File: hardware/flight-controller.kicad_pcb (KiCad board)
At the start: 4 copper layers, 70 x 70 mm, 111 parts, among them J1 USB_C_Receptacle_USB2.0_16P, J10 Screw_Terminal_01x02, J11 Micro_SD_Card_Det_Hirose_DM3AT, J12 Conn_01x03, J13 Conn_01x03, J14 Conn_01x03, J15 Conn_01x03, J16 Screw_Terminal_01x02, J17 Conn_01x04, J18 Screw_Terminal_01x02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

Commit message: finished board
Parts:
- added C39: 100nF, Capacitor_SMD:C_0402_1005Metric, F.Cu at (166.0, 114.7)
- added SET1: SW_Push, Button_Switch_SMD:SW_Push_SPST_NO_Alps_SKRK, F.Cu at (165.9, 117.0)
- BZ1: value Buzzer -> PKMCS0909E4000-R1
- J10, J16, J18, J5, J7, J9: footprint TerminalBlock_4Ucon:TerminalBlock_4Ucon_1x02_P3.50mm_Horizontal -> TerminalBlock:TerminalBlock_MaiXu_MX126-5.0-02P_1x02_P5.00mm
- moved J7 5.55 mm to (112.0, 76.5), turned to 90 degrees
- moved J16 5.05 mm to (172.0, 129.8), turned to -90 degrees
- moved J18 4.35 mm to (122.5, 73.0), turned to 0 degrees
- moved J5 4.35 mm to (156.5, 73.0), turned to 0 degrees
- moved J9 3.09 mm to (112.0, 134.2), turned to 90 degrees
- moved J10 2.86 mm to (172.0, 72.0), turned to -90 degrees
- moved C37 2.57 mm to (166.5, 131.0), turned to -90 degrees
- moved C36 2.36 mm to (166.5, 75.0), turned to -90 degrees
- moved C34 1.77 mm to (117.5, 74.0), turned to 90 degrees
- moved C35 1.60 mm to (117.5, 132.0), turned to 90 degrees
- moved C32 1.25 mm to (125.0, 78.5), turned to 0 degrees
- moved C33 1.25 mm to (159.0, 78.5), turned to 0 degrees
- moved J12 0.50 mm to (120.5, 130.5)
- moved J13 0.50 mm to (125.1, 130.5)
- moved J14 0.50 mm to (129.7, 130.5)
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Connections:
- U7 pad 89: unconnected-(U7-PB3(JTDO-Pad89) -> /SET_BTN
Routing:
- net /SET_BTN: track 0.00 -> 26.0 mm, vias 0 -> 2
- net +BATT: track 39.7 -> 43.4 mm
- net GND: track 92.8 -> 94.9 mm, vias 186 -> 188
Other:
- board text added: "+"
- board text added: "-"
- board text added: "12V"
- board text added: "3.3V"
- board text added: "CLK"
- board text added: "IO"
- board text added: "SWD"

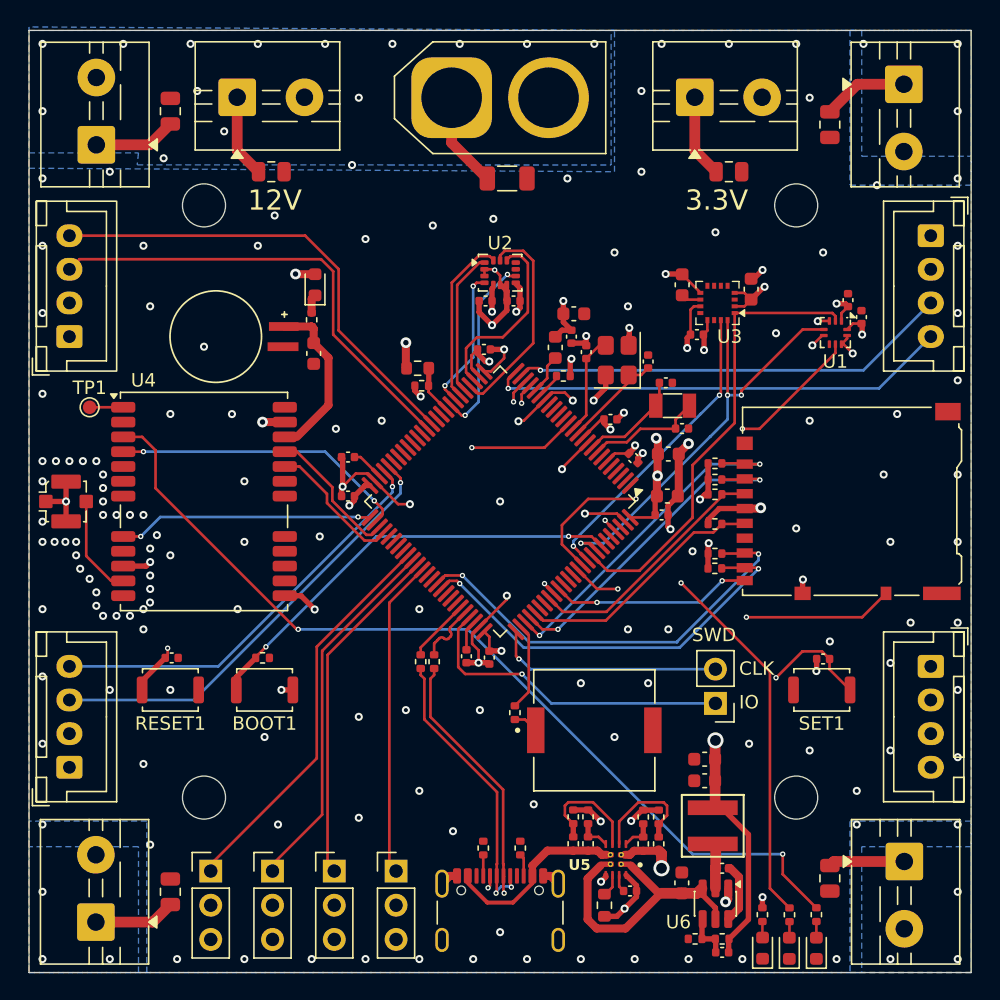
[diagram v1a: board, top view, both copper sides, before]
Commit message: added I2C pins
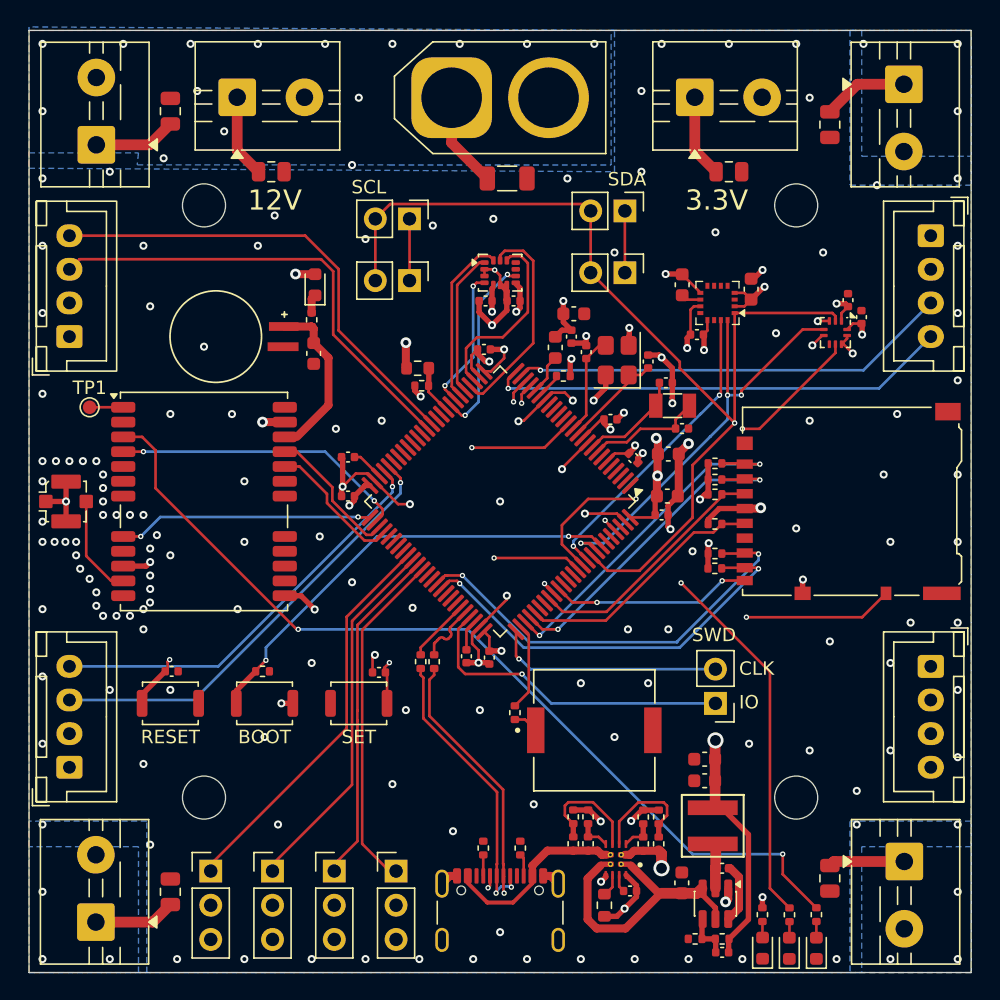
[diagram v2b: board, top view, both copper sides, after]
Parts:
- added J20: Conn_01x02, Connector_PinHeader_2.54mm:PinHeader_1x02_P2.54mm_Vertical, F.Cu at (135.3, 82.0)
- added J21: Conn_01x02, Connector_PinHeader_2.54mm:PinHeader_1x02_P2.54mm_Vertical, F.Cu at (135.3, 86.6)
- added J22: Conn_01x02, Connector_PinHeader_2.54mm:PinHeader_1x02_P2.54mm_Vertical, F.Cu at (151.3, 81.4)
- added J23: Conn_01x02, Connector_PinHeader_2.54mm:PinHeader_1x02_P2.54mm_Vertical, F.Cu at (151.3, 86.0)
- moved SET1 34.4 mm to (131.5, 118.0)
- moved C39 33.0 mm to (133.0, 115.7)
- moved BOOT1 1.00 mm to (124.5, 118.0)
- moved C11 1.00 mm to (117.6, 115.6)
- moved R16 1.00 mm to (124.3, 115.6)
- moved RESET1 1.00 mm to (117.5, 118.0)
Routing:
- net /SCL: track 34.0 -> 75.5 mm, vias 0 -> 1
- net /SDA: track 32.9 -> 71.7 mm
- net /SET_BTN: track 26.0 -> 20.6 mm
- net GND: track 94.9 -> 100.1 mm, vias 188 -> 189
- net /PWM_4: track 23.4 -> 25.1 mm
- net /BOOT: track 32.8 -> 33.7 mm
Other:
- board text added: "BOOT"
- board text added: "RESET"
- board text added: "SCL"
- board text added: "SDA"
- board text added: "SET"

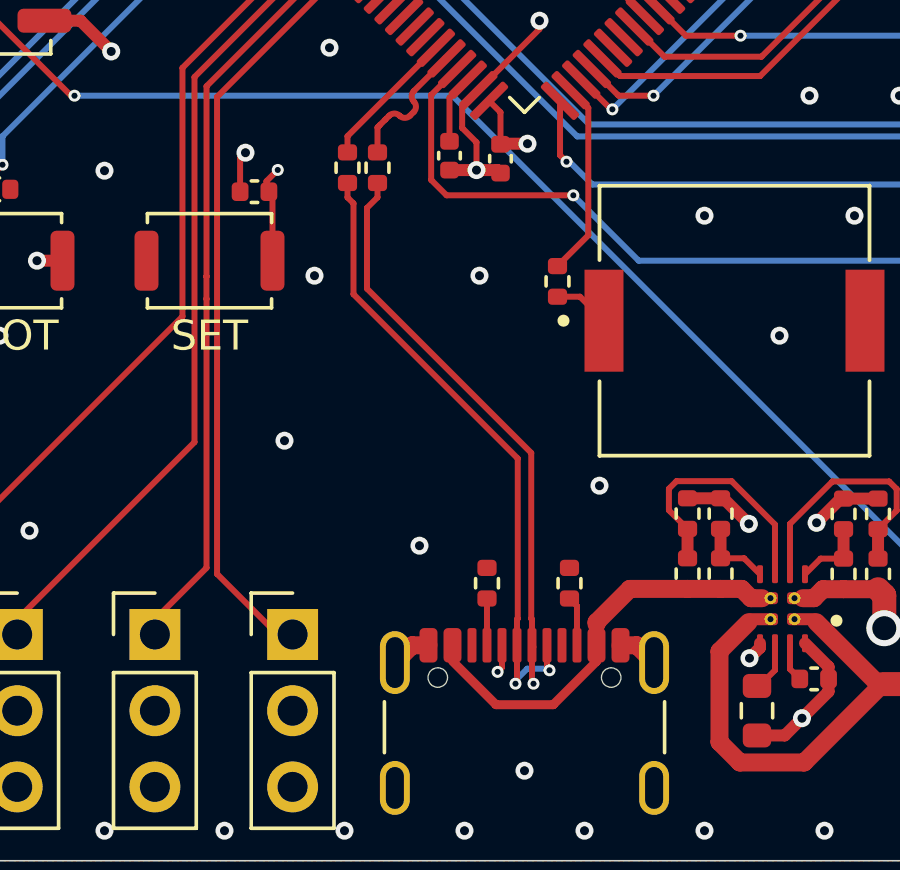
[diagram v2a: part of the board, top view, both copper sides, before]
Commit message: fixed usb plug
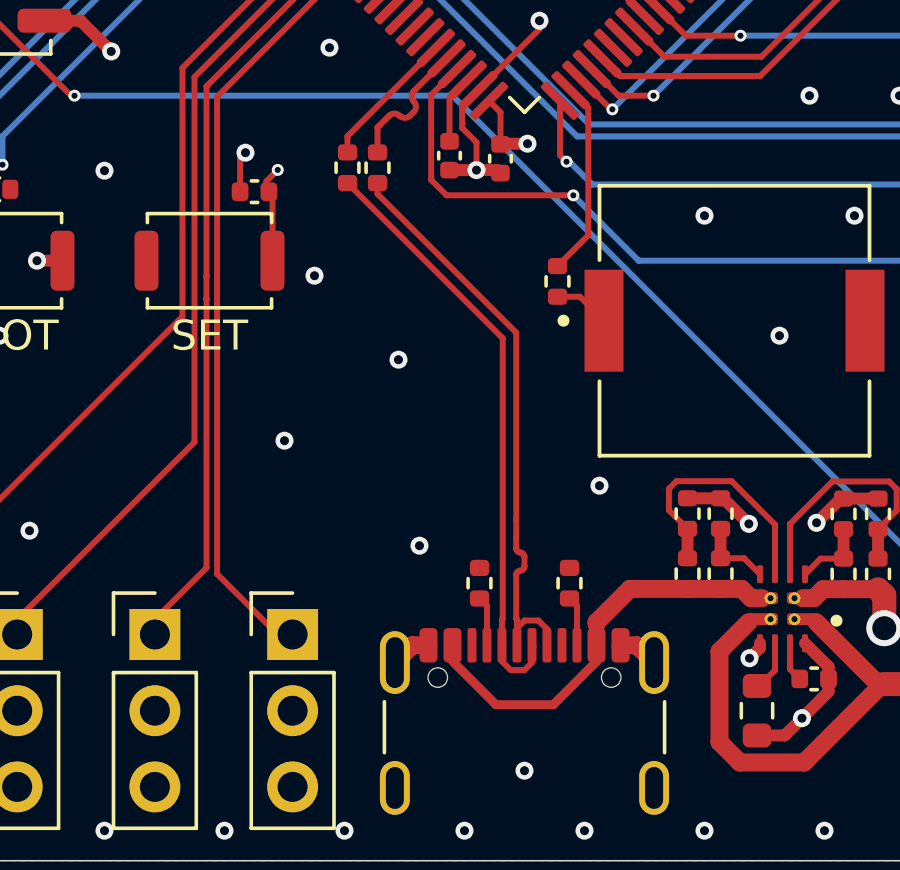
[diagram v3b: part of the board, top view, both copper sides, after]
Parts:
- moved R1 0.25 mm to (140.5, 128.8)
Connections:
- J1 pad A6: /USB_- -> /USB_+
- J1 pad A7: /USB_+ -> /USB_-
- J1 pad B6: /USB_- -> /USB_+
- J1 pad B7: /USB_+ -> /USB_-
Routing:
- net /USB_+: track 21.7 -> 20.0 mm, vias 2 -> 0
- net /USB_-: track 21.4 -> 20.0 mm, vias 2 -> 0
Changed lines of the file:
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@@
 			(layers "F.Cu" "F.Mask" "F.Paste")
 			(roundrect_rratio 0.25)
-			(net 28 "/USB_-")
+			(net 26 "/USB_+")
 			(pinfunction "D+")
 			(pintype "bidirectional")
@@
 			(layers "F.Cu" "F.Mask" "F.Paste")
 			(roundrect_rratio 0.25)
-			(net 26 "/USB_+")
+			(net 28 "/USB_-")
 			(pinfunction "D-")
 			(pintype "bidirectional")
@@
 			(layers "F.Cu" "F.Mask" "F.Paste")
 			(roundrect_rratio 0.25)
-			(net 28 "/USB_-")
+			(net 26 "/USB_+")
 			(pinfunction "D+")
 			(pintype "bidirectional")
@@
 			(layers "F.Cu" "F.Mask" "F.Paste")
 			(roundrect_rratio 0.25)
-			(net 26 "/USB_+")
+			(net 28 "/USB_-")
 			(pinfunction "D-")
 			(pintype "bidirectional")
@@
 	(footprint "Resistor_SMD:R_0402_1005Metric"
 		(layer "F.Cu")
-		(at 140.75 128.75 90)
+		(at 140.5 128.75 90)
 		(descr "Resistor SMD 0402 (1005 Metric), square (rectangular) end terminal, IPC-7351 nominal, (Body size source: IPC-SM-782 page 72, https://www.pcb-3d.com/wordpress/wp-content/uploads/ipc-sm-782a_amendment_1_and_2.pdf), generated with kicad-footprint-generator")
 		(tags "resistor")
@@
 	)
 	(via
-		(at 140.5 118.5)
+		(at 137.8 121.3)
 		(size 0.6)
 		(drill 0.3)
@@
 	)
 	(segment
-		(start 142.225 129.932499)
-		(end 142.25 129.957499)
+		(start 142.75 130.281888)
+		(end 142.75 130.82)
 		(width 0.2)
 		(layer "F.Cu")
@@
 	)
 	(segment
-		(start 136.75 116.24)
-		(end 136.75 118.931802)
+		(start 141.725 127.265204)
+		(end 141.725 126.605964)
 		(width 0.2)
 		(layer "F.Cu")
@@
 	)
 	(segment
-		(start 136.75 118.931802)
-		(end 142.225 124.406802)
+		(start 137.1 115.773602)
+		(end 137.1 115.409999)
 		(width 0.2)
 		(layer "F.Cu")
@@
 	)
 	(segment
-		(start 141.25 131.558683)
-		(end 141.103508 131.705175)
+		(start 141.75 130.245001)
+		(end 142.001001 129.994)
 		(width 0.2)
 		(layer "F.Cu")
@@
 	)
 	(segment
-		(start 137.1 115.409999)
-		(end 137.1 115.89)
+		(start 141.725 127.591352)
+		(end 141.725 127.265204)
 		(width 0.2)
 		(layer "F.Cu")
@@
 	)
 	(segment
-		(start 142.25 132.049997)
-		(end 142.300003 132.1)
+		(start 141.75 129.957499)
+		(end 141.725 129.932499)
 		(width 0.2)
 		(layer "F.Cu")
@@
 	)
 	(segment
-		(start 142.225 124.406802)
-		(end 142.225 129.932499)
+		(start 141.998852 128.191352)
+		(end 141.998852 127.865204)
 		(width 0.2)
 		(layer "F.Cu")
@@
 	)
 	(segment
-		(start 142.25 129.957499)
-		(end 142.25 130.82)
+		(start 141.75 130.82)
+		(end 141.75 130.245001)
 		(width 0.2)
 		(layer "F.Cu")
@@
 	)
 	(segment
-		(start 141.25 130.82)
-		(end 141.25 131.558683)
+		(start 141.725 126.605964)
+		(end 141.725 120.398602)
 		(width 0.2)
 		(layer "F.Cu")
@@
 	)
 	(segment
-		(start 142.3 130.87)
-		(end 142.25 130.82)
+		(start 141.725 120.398602)
+		(end 137.1 115.773602)
 		(width 0.2)
 		(layer "F.Cu")
@@
 	)
 	(segment
-		(start 137.1 115.89)
-		(end 136.75 116.24)
+		(start 142.462112 129.994)
+		(end 142.75 130.281888)
 		(width 0.2)
 		(layer "F.Cu")
@@
 	)
 	(segment
-		(start 142.25 130.82)
-		(end 142.25 132.049997)
+		(start 142.001001 129.994)
+		(end 142.462112 129.994)
 		(width 0.2)
 		(layer "F.Cu")
 		(net 26)
 	)
-	(via
-		(at 141.103508 131.705175)
-		(size 0.4)
-		(drill 0.2)
-		(layers "F.Cu" "B.Cu")
-		(net 26)
-	)
-	(via
-		(at 142.300003 132.1)
-		(size 0.4)
-		(drill 0.2)
-		(layers "F.Cu" "B.Cu")
-		(net 26)
-	)
 	(segment
-		(start 141.999 131.599)
-		(end 142.300003 131.900003)
+		(start 141.725 129.932499)
+		(end 141.725 128.465204)
 		(width 0.2)
-		(layer "In2.Cu")
+		(layer "F.Cu")
 		(net 26)
 	)
 	(segment
-		(start 141.103508 131.705175)
-		(end 141.209683 131.599)
+		(start 141.75 130.82)
+		(end 141.75 129.957499)
 		(width 0.2)
-		(layer "In2.Cu")
+		(layer "F.Cu")
 		(net 26)
 	)
-	(segment
-		(start 142.300003 131.900003)
-		(end 142.300003 132.1)
+	(arc
+		(start 141.998852 127.865204)
+		(mid 141.958747 127.768383)
+		(end 141.861926 127.728278)
 		(width 0.2)
-		(layer "In2.Cu")
+		(layer "F.Cu")
 		(net 26)
 	)
-	(segment
-		(start 141.209683 131.599)
-		(end 141.999 131.599)
+	(arc
+		(start 141.861926 127.728278)
+		(mid 141.765105 127.688173)
+		(end 141.725 127.591352)
 		(width 0.2)
-		(layer "In2.Cu")
+		(layer "F.Cu")
 		(net 26)
 	)
-	(segment
-		(start 140.75 130.82)
-		(end 140.75 129.26)
+	(arc
+		(start 141.861926 128.328278)
+		(mid 141.958747 128.288173)
+		(end 141.998852 128.191352)
 		(width 0.2)
 		(layer "F.Cu")
-		(net 27)
+		(net 26)
 	)
-	(segment
-		(start 141.775 124.593198)
-		(end 136.3 119.118198)
+	(arc
+		(start 141.725 128.465204)
+		(mid 141.765105 128.368383)
+		(end 141.861926 128.328278)
 		(width 0.2)
 		(layer "F.Cu")
-		(net 28)
+		(net 26)
 	)
 	(segment
-		(start 142.75 130.82)
-		(end 142.75 131.568764)
+		(start 140.75 129.51)
+		(end 140.5 129.26)
 		(width 0.2)
 		(layer "F.Cu")
-		(net 28)
+		(net 27)
 	)
 	(segment
-		(start 136.3 116.09)
-		(end 136.1 115.89)
+		(start 140.75 130.82)
+		(end 140.75 129.51)
 		(width 0.2)
 		(layer "F.Cu")
-		(net 28)
+		(net 27)
 	)
 	(segment
-		(start 141.775 129.932499)
-		(end 141.775 124.593198)
+		(start 141.275 129.932499)
+		(end 141.25 129.957499)
 		(width 0.2)
 		(layer "F.Cu")
@@
 	)
 	(segment
-		(start 136.1 115.89)
-		(end 136.1 115.409999)
+		(start 141.25 131.358112)
+		(end 141.25 130.82)
 		(width 0.2)
 		(layer "F.Cu")
@@
 	)
 	(segment
-		(start 141.75 130.82)
-		(end 141.75 129.957499)
+		(start 136.1 115.409999)
+		(end 141.275 120.584999)
 		(width 0.2)
 		(layer "F.Cu")
@@
 	)
 	(segment
-		(start 141.75 132.05)
-		(end 141.7 132.1)
+		(start 141.998999 131.646)
+		(end 141.537888 131.646)
 		(width 0.2)
 		(layer "F.Cu")
@@
 	)
 	(segment
-		(start 142.75 131.568764)
-		(end 142.833804 131.652568)
+		(start 142.25 130.82)
+		(end 142.25 131.394999)
 		(width 0.2)
 		(layer "F.Cu")
@@
 	)
 	(segment
-		(start 136.3 119.118198)
-		(end 136.3 116.09)
+		(start 141.25 129.957499)
+		(end 141.25 130.82)
 		(width 0.2)
 		(layer "F.Cu")
@@
 	)
 	(segment
-		(start 141.75 130.82)
-		(end 141.75 132.05)
+		(start 142.25 131.394999)
+		(end 141.998999 131.646)
 		(width 0.2)
 		(layer "F.Cu")
@@
 	)
 	(segment
-		(start 141.75 129.957499)
-		(end 141.775 129.932499)
+		(start 141.537888 131.646)
+		(end 141.25 131.358112)
 		(width 0.2)
 		(layer "F.Cu")
 		(net 28)
 	)
-	(via
-		(at 142.833804 131.652568)
-		(size 0.4)
-		(drill 0.2)
-		(layers "F.Cu" "B.Cu")
-		(net 28)
-	)
-	(via
-		(at 141.7 132.1)
-		(size 0.4)
-		(drill 0.2)
-		(layers "F.Cu" "B.Cu")
-		(net 28)
-	)
-	(segment
-		(start 141.7 131.991482)
-		(end 141.7 132.1)
-		(width 0.2)
-		(layer "B.Cu")
-		(net 28)
-	)
-	(segment
-		(start 142.092482 131.599)
-		(end 141.7 131.991482)
-		(width 0.2)
-		(layer "B.Cu")
-		(net 28)
-	)
 	(segment
-		(start 142.780236 131.599)
-		(end 142.092482 131.599)
+		(start 141.275 120.584999)
+		(end 141.275 129.932499)
 		(width 0.2)
-		(layer "B.Cu")
+		(layer "F.Cu")
 		(net 28)
 	)
 	(segment
-		(start 142.833804 131.652568)
-		(end 142.780236 131.599)
+		(start 142.3 130.87)
+		(end 142.25 130.82)
 		(width 0.2)
-		(layer "B.Cu")
+		(layer "F.Cu")
 		(net 28)
 	)
@@
 		)
 	)
+	(generated
+		(type tuning_pattern)
+		(name "Tuning Pattern")
+		(layer "F.Cu")
+		(base_line
+			(pts
+				(xy 141.725 128.465204) (xy 141.725 126.605964)
+			)
+		)
+		(base_line_coupled
+			(pts
+				(xy 141.275 122.19934) (xy 141.275 122.018189)
+			)
+		)
+		(corner_radius_percent 80)
+		(end
+			(xy 141.725 126.605964)
+		)
+		(initial_side "right")
+		(last_diff_pair_gap 0.18)
+		(last_netname "/USB_+")
+		(last_status "tuned")
+		(last_track_width 0.2)
+		(last_tuning "-0.0000 mm (tuned)")
+		(max_amplitude 1)
+		(min_amplitude 0.2)
+		(min_spacing 0.6)
+		(origin
+			(xy 141.725 128.465204)
+		)
+		(override_custom_rules no)
+		(rounded yes)
+		(single_sided no)
+		(target_length 1000000)
+		(target_length_max 1000000)
+		(target_length_min 0)
+		(target_skew 0)
+		(target_skew_max 0.1)
+		(target_skew_min -0.1)
+		(tuning_mode "diff_pair_skew")
+		(members "0b208a13-e065-4588-9ed5-f39528cc193d" "2cb9b9e5-244c-416e-be72-99701497e52d"
+			"3118765a-8bdb-40dc-93fe-ec1dbc5a71dd" "3bae983b-057e-4378-aa41-0a10a419d79f"
+			"8954a298-06cc-4e8c-820e-a3303c16cde6" "9e7ad060-a8d3-4bd9-b4aa-a9479a469fc6"
+			"b27208e8-2e01-45e8-83c2-04742e1c18b1"
+		)
+	)
